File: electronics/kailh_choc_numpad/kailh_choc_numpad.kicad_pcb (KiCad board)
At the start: 2 copper layers, 89.5 x 88 mm, 83 parts

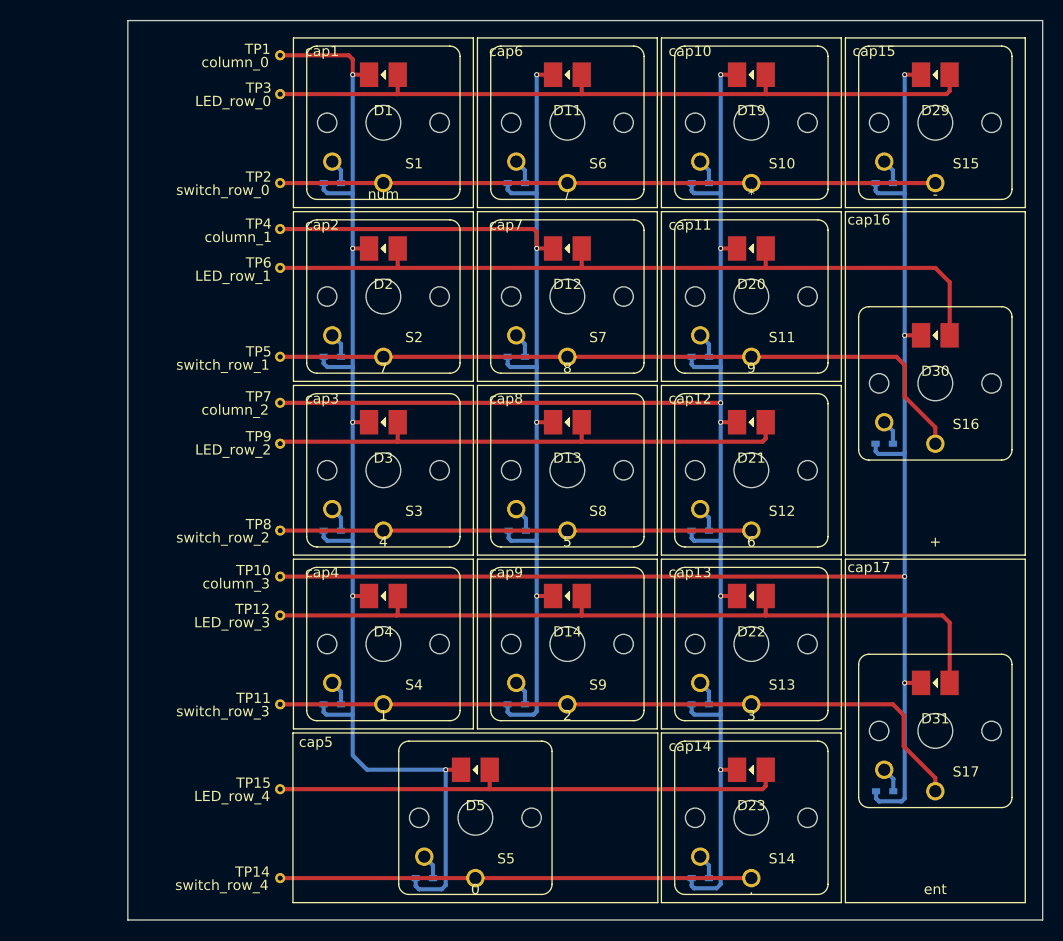
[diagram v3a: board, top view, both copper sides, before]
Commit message: added, placed and routed ESD diodes
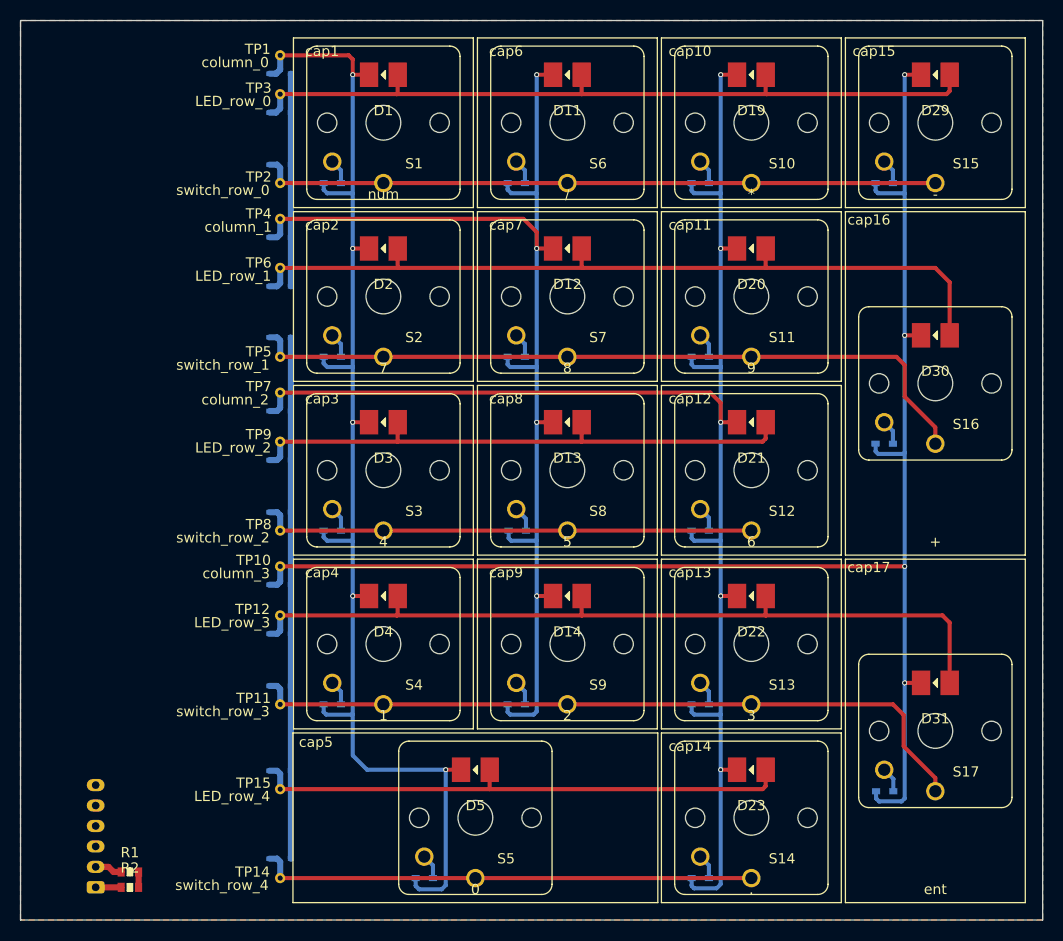
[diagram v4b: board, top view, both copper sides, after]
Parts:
- added D35: SD05, Diode_SMD:D_SOD-323, B.Cu at (159.9, 75.2)
- added D36: SD05, Diode_SMD:D_SOD-323, B.Cu at (159.9, 84.1)
- added D37: SD05, Diode_SMD:D_SOD-323, B.Cu at (159.9, 79.0)
- added D38: SD05, Diode_SMD:D_SOD-323, B.Cu at (159.9, 91.2)
- added D39: SD05, Diode_SMD:D_SOD-323, B.Cu at (159.9, 101.0)
- added D40: SD05, Diode_SMD:D_SOD-323, B.Cu at (159.9, 96.0)
- added D41: SD05, Diode_SMD:D_SOD-323, B.Cu at (159.9, 108.2)
- added D42: SD05, Diode_SMD:D_SOD-323, B.Cu at (159.9, 118.1)
- added D43: SD05, Diode_SMD:D_SOD-323, B.Cu at (159.9, 113.0)
- added D44: SD05, Diode_SMD:D_SOD-323, B.Cu at (159.9, 125.2)
- added D45: SD05, Diode_SMD:D_SOD-323, B.Cu at (159.9, 135.1)
- added D46: SD05, Diode_SMD:D_SOD-323, B.Cu at (159.9, 130.0)
- added D47: SD05, Diode_SMD:D_SOD-323, B.Cu at (159.9, 152.0)
- added D48: SD05, Diode_SMD:D_SOD-323, B.Cu at (159.9, 143.4)
- added J1: Conn_01x06, Connector_JST:JST_PH_S6B-PH-K_1x06_P2.00mm_Horizontal, B.Cu at (141.8, 154.8)
- added R1: 0, SquantorRcl:R_0603_hand, F.Cu at (145.2, 153.3)
- added R2: 0, SquantorRcl:R_0603_hand, F.Cu at (145.2, 154.8)
- moved TP10 1.00 mm to (159.9, 123.4)
- moved TP4 1.00 mm to (159.9, 89.4)
- moved TP7 1.00 mm to (159.9, 106.4)
- moved TP9 0.20 mm to (159.9, 111.2)
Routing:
- net VSS: track 0.00 -> 71.8 mm
- net /column_2: track 149.0 -> 154.0 mm, vias 6 -> 5
- net /column_1: track 110.3 -> 113.4 mm
- net /switch_row_1: track 70.4 -> 73.1 mm
- net /switch_row_4: track 46.1 -> 48.9 mm
- net Net-(J1-Pad2): track 0.00 -> 2.71 mm
- net /switch_row_3: track 70.2 -> 72.8 mm
- net /switch_row_0: track 64.1 -> 66.8 mm
- net /LED_row_3: track 77.4 -> 80.1 mm
- net /switch_row_2: track 46.1 -> 48.8 mm
- net /LED_row_1: track 77.1 -> 79.7 mm
- net /LED_row_4: track 51.1 -> 53.8 mm
- net /column_3: track 147.9 -> 150.6 mm
- net /column_0: track 122.9 -> 125.6 mm
- net /LED_row_0: track 73.0 -> 75.6 mm
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- added copper zone on F.Cu, net VSS
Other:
- board size 89.5 x 88 mm -> 100 x 88 mm

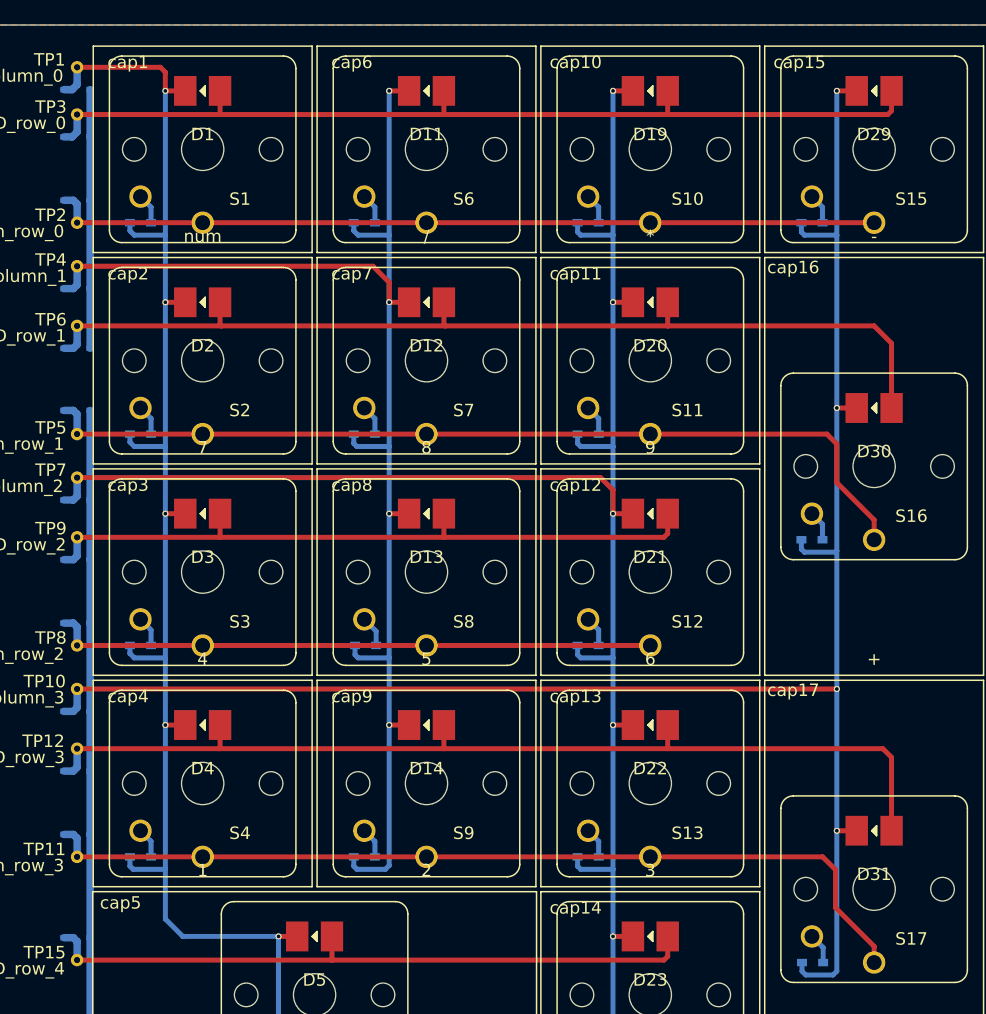
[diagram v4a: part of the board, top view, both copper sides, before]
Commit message: placed resistors, now routing needed
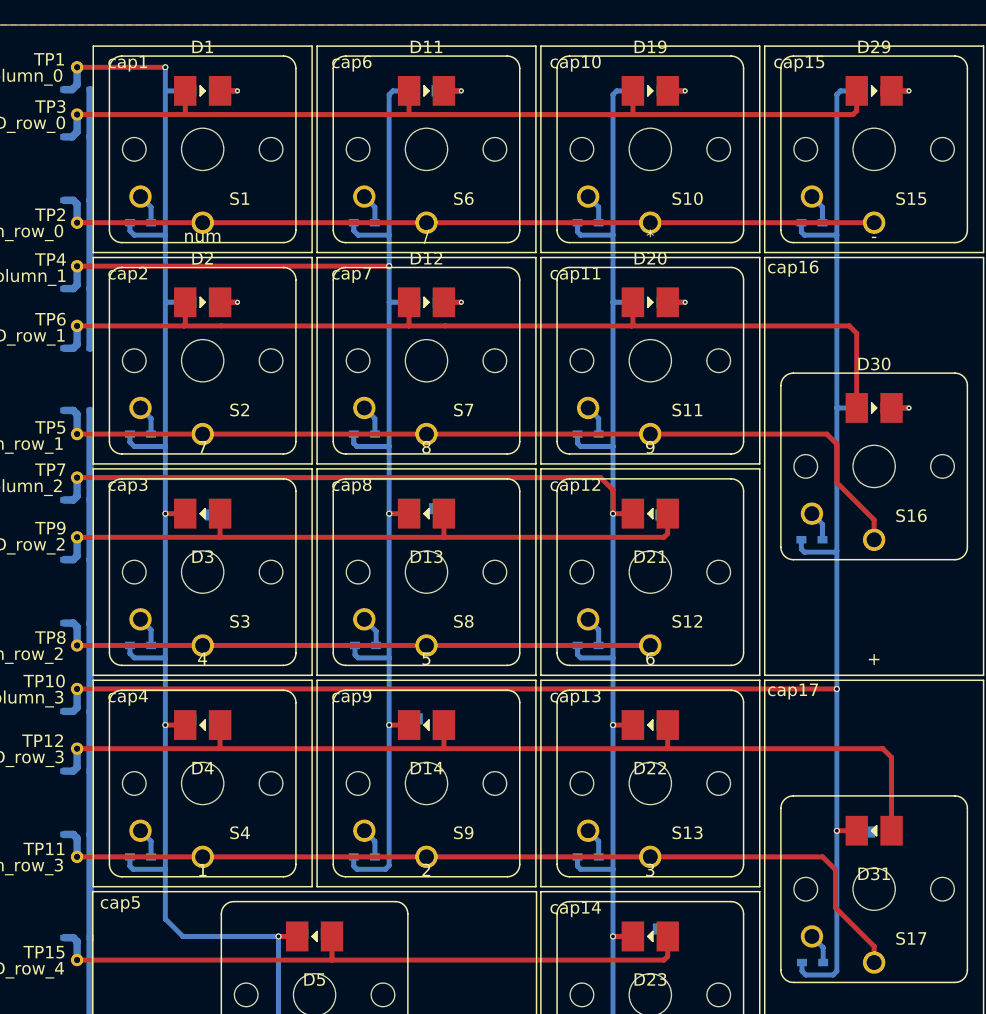
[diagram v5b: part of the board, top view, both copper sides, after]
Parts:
- added R10: 470, SquantorRcl:R_0603_hand, B.Cu at (179.0, 143.1)
- added R11: 470, SquantorRcl:R_0603_hand, B.Cu at (188.0, 92.3)
- added R12: 470, SquantorRcl:R_0603_hand, B.Cu at (187.7, 108.9)
- added R13: 470, SquantorRcl:R_0603_hand, B.Cu at (188.2, 125.8)
- added R14: 470, SquantorRcl:R_0603_hand, B.Cu at (206.0, 92.3)
- added R15: 470, SquantorRcl:R_0603_hand, B.Cu at (205.9, 109.4)
- added R16: 470, SquantorRcl:R_0603_hand, B.Cu at (206.0, 126.3)
- added R17: 470, SquantorRcl:R_0603_hand, B.Cu at (205.7, 142.7)
- added R18: 470, SquantorRcl:R_0603_hand, B.Cu at (224.0, 100.8)
- added R19: 470, SquantorRcl:R_0603_hand, B.Cu at (224.6, 134.9)
- added R3: 470, SquantorRcl:R_0603_hand, B.Cu at (170.0, 75.3)
- added R4: 470, SquantorRcl:R_0603_hand, B.Cu at (187.9, 75.3)
- added R5: 470, SquantorRcl:R_0603_hand, B.Cu at (206.0, 75.3)
- added R6: 470, SquantorRcl:R_0603_hand, B.Cu at (224.0, 75.3)
- added R7: 470, SquantorRcl:R_0603_hand, B.Cu at (170.0, 92.3)
- added R8: 470, SquantorRcl:R_0603_hand, B.Cu at (169.7, 109.4)
- added R9: 470, SquantorRcl:R_0603_hand, B.Cu at (170.0, 125.9)
- turned D1 to 180 degrees
- turned D11 to 180 degrees
- turned D12 to 180 degrees
- turned D19 to 180 degrees
- turned D2 to 180 degrees
- turned D20 to 180 degrees
- turned D29 to 180 degrees
- turned D30 to 180 degrees
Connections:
- D1 pad 1: /column_0 -> Net-(D1-Pad1)
- D11 pad 1: /column_1 -> Net-(D11-Pad1)
- D12 pad 1: /column_1 -> Net-(D12-Pad1)
- D13 pad 1: /column_1 -> Net-(D13-Pad1)
- D14 pad 1: /column_1 -> Net-(D14-Pad1)
- D19 pad 1: /column_2 -> Net-(D19-Pad1)
- D2 pad 1: /column_0 -> Net-(D2-Pad1)
- D20 pad 1: /column_2 -> Net-(D20-Pad1)
- D21 pad 1: /column_2 -> Net-(D21-Pad1)
- D22 pad 1: /column_2 -> Net-(D22-Pad1)
- D23 pad 1: /column_2 -> Net-(D23-Pad1)
- D29 pad 1: /column_3 -> Net-(D29-Pad1)
- D3 pad 1: /column_0 -> Net-(D3-Pad1)
- D30 pad 1: /column_3 -> Net-(D30-Pad1)
- D31 pad 1: /column_3 -> Net-(D31-Pad1)
- D4 pad 1: /column_0 -> Net-(D4-Pad1)
- D5 pad 1: /column_0 -> Net-(D5-Pad1)
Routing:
- net Net-(D11-Pad1): track 0.00 -> 3.45 mm, vias 0 -> 1
- net Net-(D30-Pad1): track 0.00 -> 3.35 mm, vias 0 -> 1
- net Net-(D29-Pad1): track 0.00 -> 3.35 mm, vias 0 -> 1
- net Net-(D20-Pad1): track 0.00 -> 3.35 mm, vias 0 -> 1
- net Net-(D2-Pad1): track 0.00 -> 3.35 mm, vias 0 -> 1
- net Net-(D19-Pad1): track 0.00 -> 3.35 mm, vias 0 -> 1
- net Net-(D12-Pad1): track 0.00 -> 3.35 mm, vias 0 -> 1
- net Net-(D1-Pad1): track 0.00 -> 3.35 mm, vias 0 -> 1
- net /LED_row_0: track 75.6 -> 72.8 mm
- net /LED_row_1: track 79.7 -> 77.4 mm
- net /column_0: track 125.6 -> 126.9 mm, vias 5 -> 4
- net /column_1: track 113.4 -> 112.1 mm, vias 4 -> 3
- net /column_2: track 154.0 -> 154.9 mm, vias 5 -> 3
- net /column_3: track 150.6 -> 151.5 mm, vias 4 -> 2

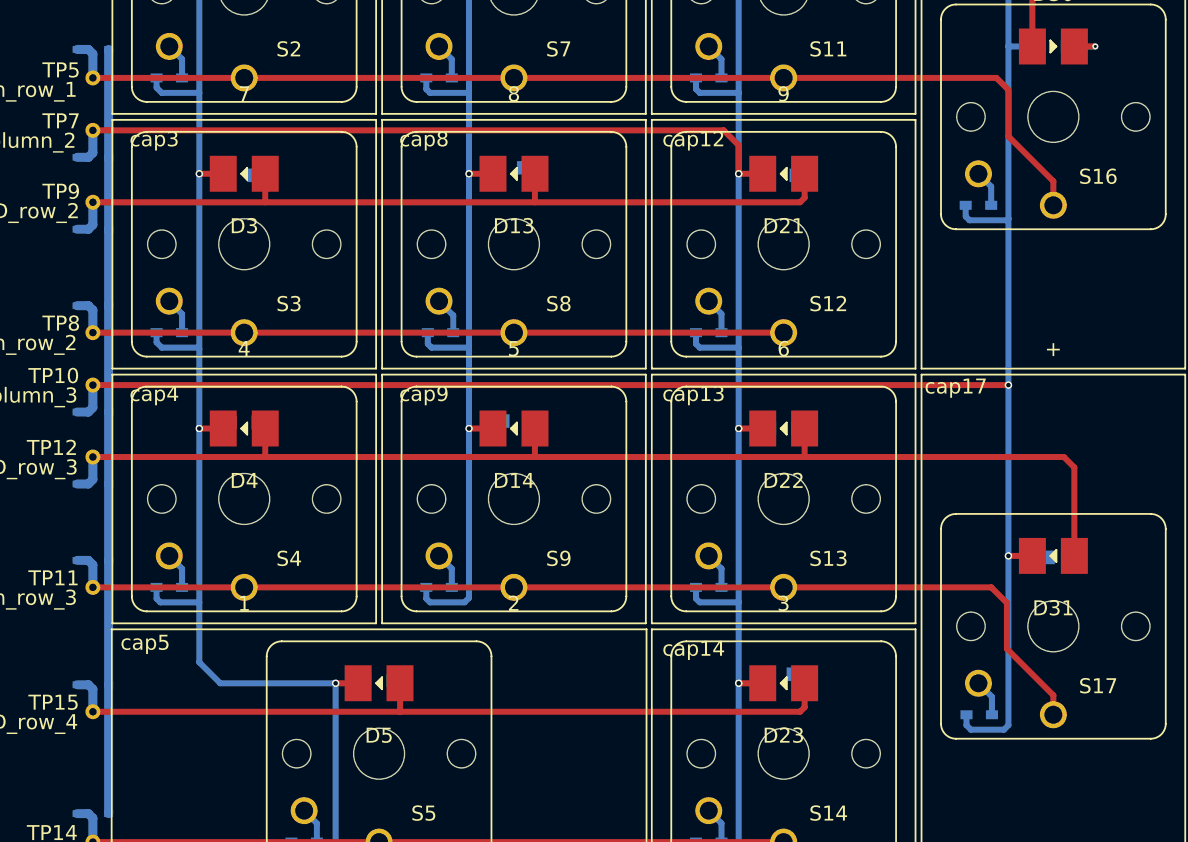
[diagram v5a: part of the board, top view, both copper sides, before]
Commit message: placed and routed LED resistors
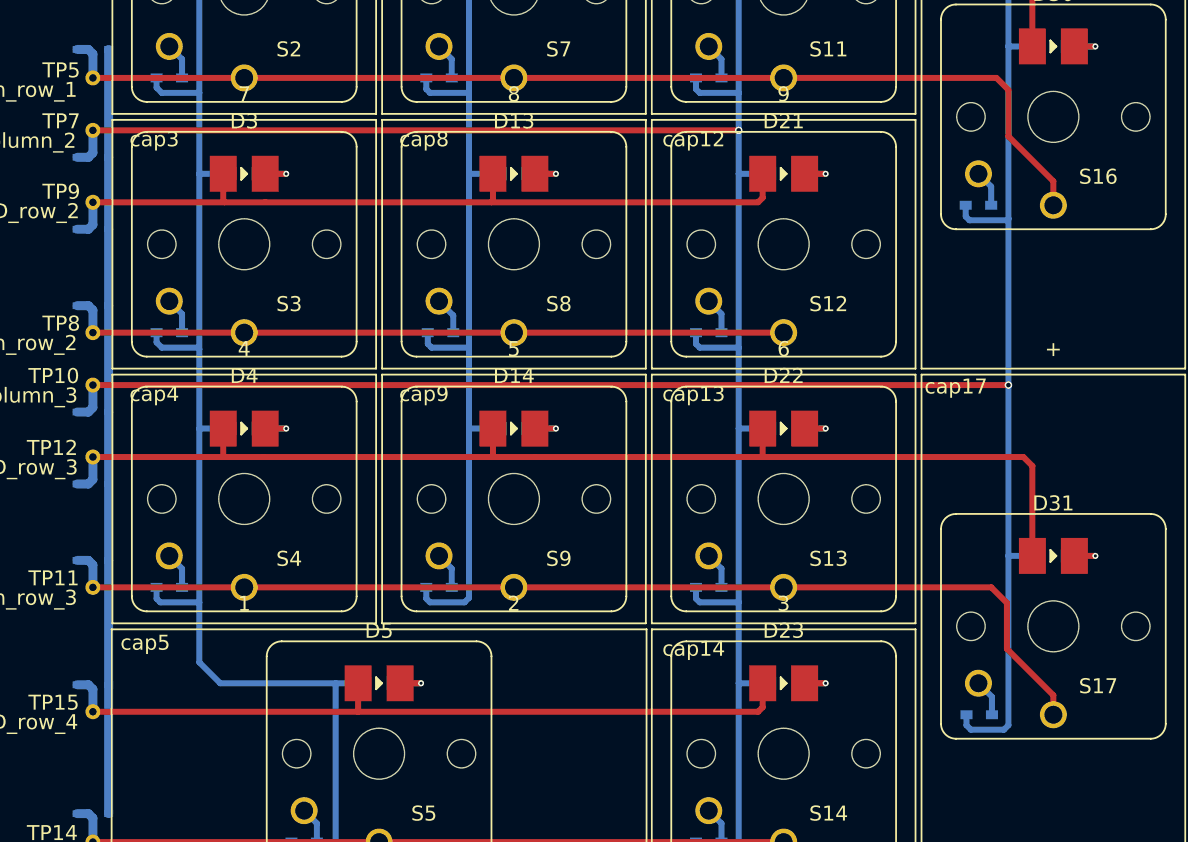
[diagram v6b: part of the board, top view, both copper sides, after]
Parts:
- moved R17 0.67 mm to (206.0, 143.3)
- moved R19 0.61 mm to (224.0, 134.8)
- moved R13 0.54 mm to (188.0, 126.3)
- moved R12 0.50 mm to (188.0, 109.3)
- moved R9 0.40 mm to (170.0, 126.3)
- moved R8 0.32 mm to (170.0, 109.3)
- moved R10 0.20 mm to (179.0, 143.3)
- moved R15 0.14 mm to (206.0, 109.3)
- turned D13 to 180 degrees
- turned D14 to 180 degrees
- turned D21 to 180 degrees
- turned D22 to 180 degrees
- turned D23 to 180 degrees
- turned D3 to 180 degrees
- turned D31 to 180 degrees
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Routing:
- net Net-(D5-Pad1): track 0.00 -> 3.35 mm, vias 0 -> 1
- net Net-(D4-Pad1): track 0.00 -> 3.35 mm, vias 0 -> 1
- net Net-(D31-Pad1): track 0.00 -> 3.35 mm, vias 0 -> 1
- net Net-(D3-Pad1): track 0.00 -> 3.35 mm, vias 0 -> 1
- net Net-(D23-Pad1): track 0.00 -> 3.35 mm, vias 0 -> 1
- net Net-(D22-Pad1): track 0.00 -> 3.35 mm, vias 0 -> 1
- net Net-(D21-Pad1): track 0.00 -> 3.35 mm, vias 0 -> 1
- net Net-(D14-Pad1): track 0.00 -> 3.35 mm, vias 0 -> 1
- net Net-(D13-Pad1): track 0.00 -> 3.35 mm, vias 0 -> 1
- net /LED_row_4: track 53.8 -> 51.0 mm
- net /LED_row_3: track 80.1 -> 77.4 mm
- net /LED_row_2: track 55.7 -> 53.0 mm
- net /column_0: track 126.9 -> 128.6 mm, vias 4 -> 1
- net /column_1: track 112.1 -> 113.2 mm, vias 3 -> 1
- net /column_2: track 154.9 -> 154.2 mm, vias 3 -> 1
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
